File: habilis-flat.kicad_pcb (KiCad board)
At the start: 2 copper layers, 164.5 x 172.8 mm, 74 parts, among them J1 AudioJack4, SW1 MX, SW10 MX, SW11 MX, SW12 MX, SW13 MX, SW14 MX, SW15 MX, SW16 MX, SW17 MX, SW18 MX, SW19 MX, SW2 MX, SW20 MX, SW21 MX, SW22 MX, SW23 MX, SW24 MX, SW25 MX, SW26 MX, SW27 MX, SW28 MX, SW29 MX, SW3 MX, SW30 MX, SW31 MX, SW32 MX, SW33 MX, SW34 MX, SW35 MX, SW4 MX, SW5 MX, SW6 MX, SW7 MX, SW8 MX, SW9 MX, U1 ProMicro

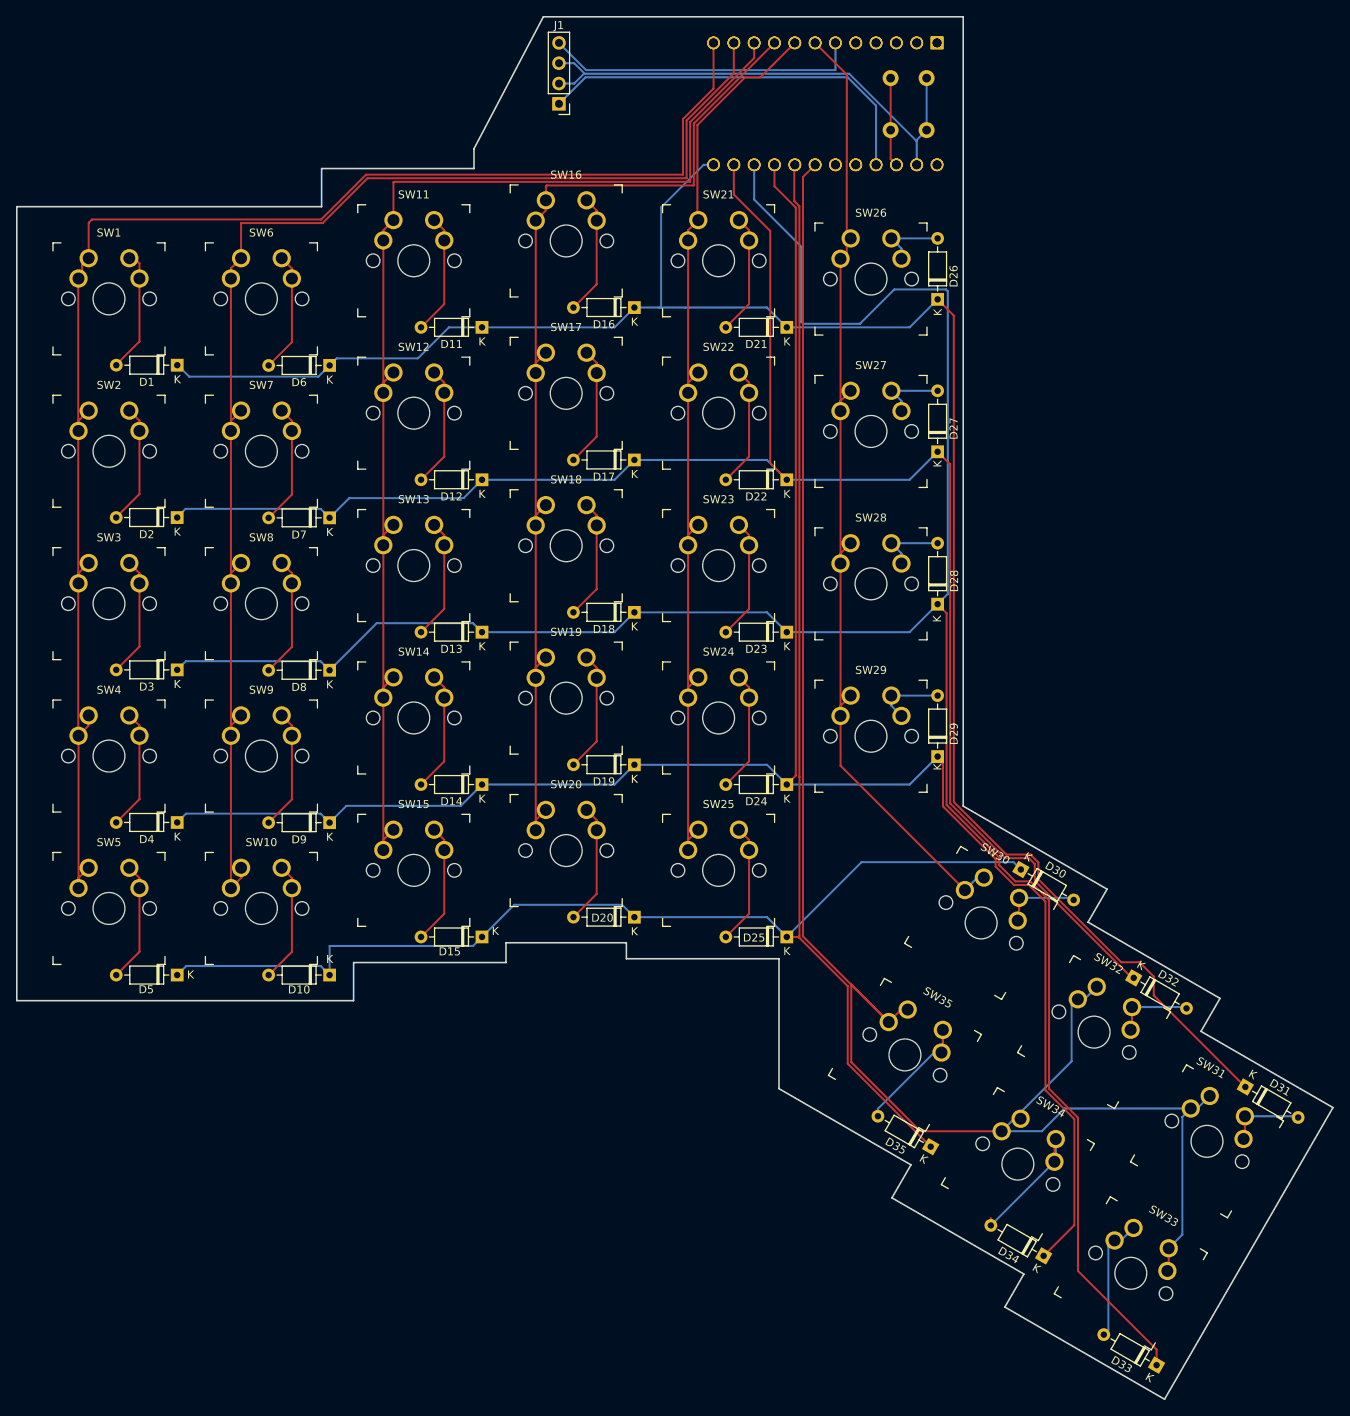
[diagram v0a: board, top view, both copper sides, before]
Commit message: Add mounting holes, simplify silkscreen
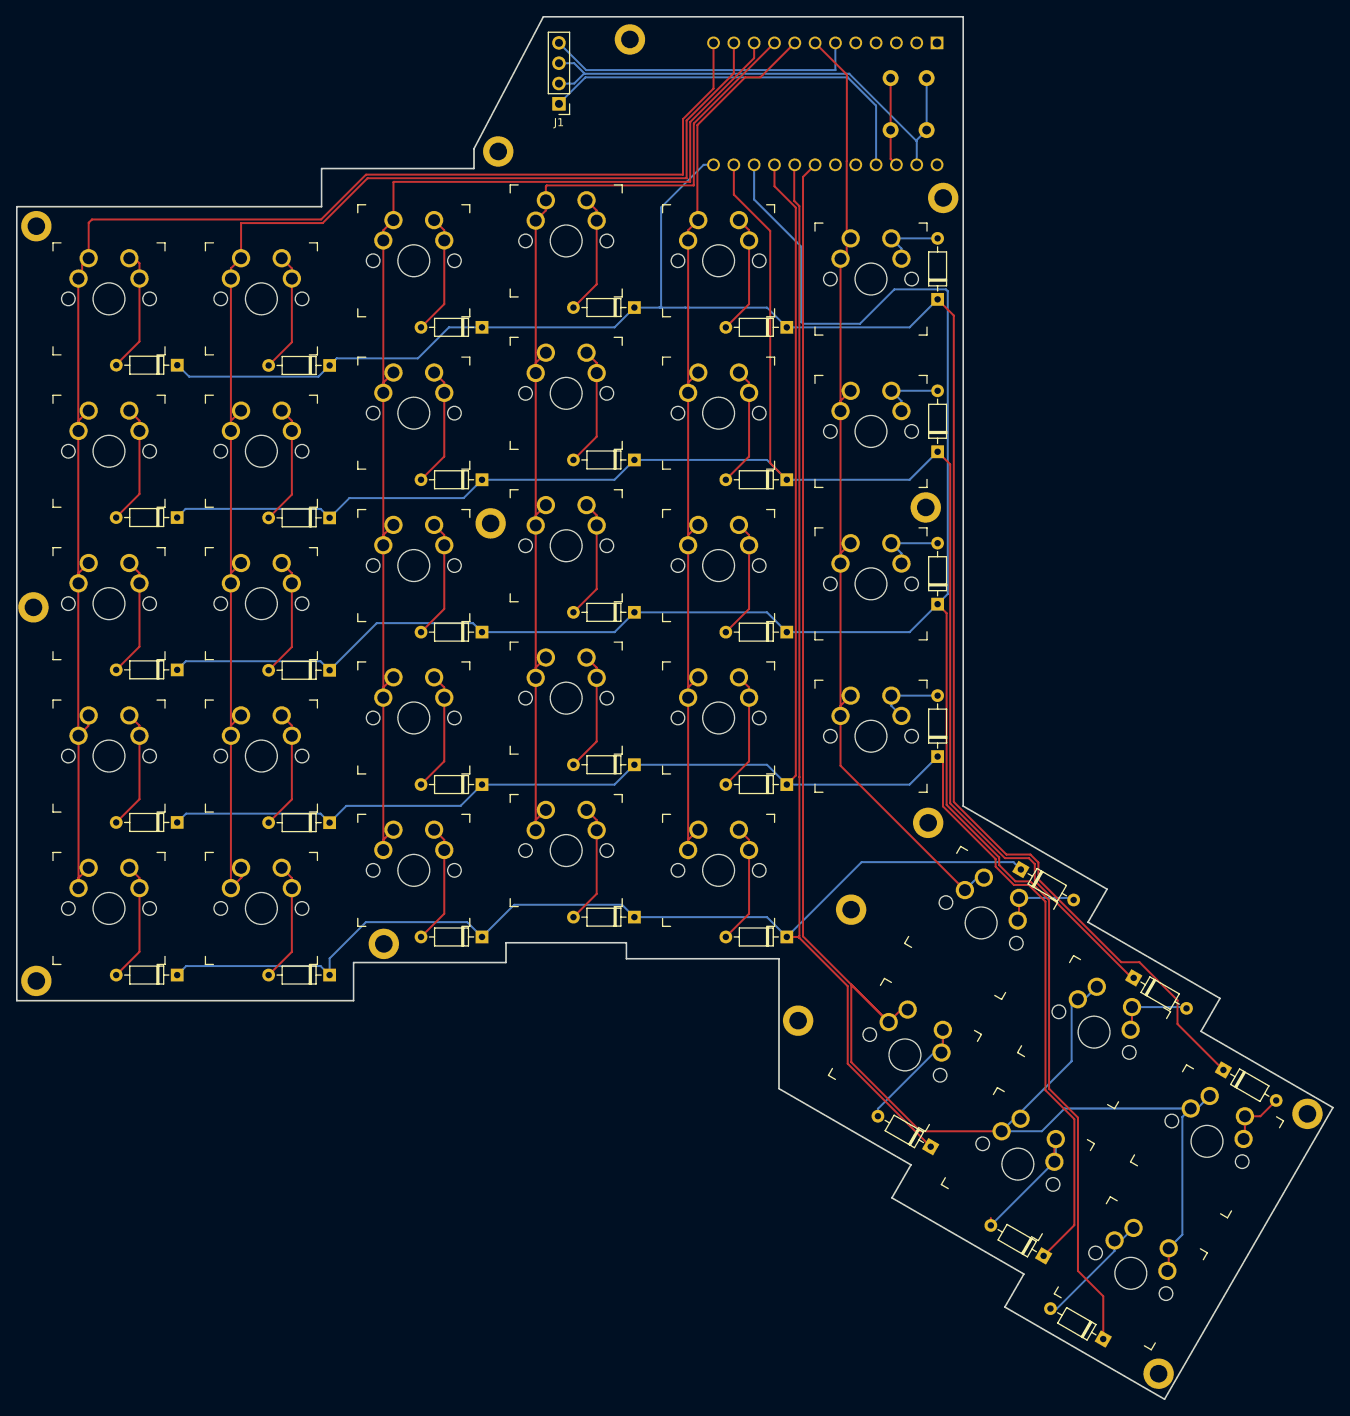
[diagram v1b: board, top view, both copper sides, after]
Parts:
- removed the U1 at (87.0, -19.3)
- added REF**: MountingHole_2.2mm_M2_DIN965_Pad_NO_Silkscreem, project-components:MountingHole_2.2mm_M2_DIN965_Pad_NO_Silkscreem, F.Cu at (99.6, 31.2)
- added REF**: MountingHole_2.2mm_M2_DIN965_Pad_NO_Silkscreem, project-components:MountingHole_2.2mm_M2_DIN965_Pad_NO_Silkscreem, F.Cu at (31.8, 85.7)
- added REF**: MountingHole_2.2mm_M2_DIN965_Pad_NO_Silkscreem, project-components:MountingHole_2.2mm_M2_DIN965_Pad_NO_Silkscreem, F.Cu at (99.9, 70.6)
- added REF**: MountingHole_2.2mm_M2_DIN965_Pad_NO_Silkscreem, project-components:MountingHole_2.2mm_M2_DIN965_Pad_NO_Silkscreem, F.Cu at (-11.6, -4.00)
- added REF**: MountingHole_2.2mm_M2_DIN965_Pad_NO_Silkscreem, project-components:MountingHole_2.2mm_M2_DIN965_Pad_NO_Silkscreem, F.Cu at (-11.6, 90.3)
- added REF**: MountingHole_2.2mm_M2_DIN965_Pad_NO_Silkscreem, project-components:MountingHole_2.2mm_M2_DIN965_Pad_NO_Silkscreem, F.Cu at (147.3, 107.0)
- added REF**: MountingHole_2.2mm_M2_DIN965_Pad_NO_Silkscreem, project-components:MountingHole_2.2mm_M2_DIN965_Pad_NO_Silkscreem, F.Cu at (46.1, -13.3)
- added REF**: MountingHole_2.2mm_M2_DIN965_Pad_NO_Silkscreem, project-components:MountingHole_2.2mm_M2_DIN965_Pad_NO_Silkscreem, F.Cu at (83.6, 95.3)
- added REF**: MountingHole_2.2mm_M2_DIN965_Pad_NO_Silkscreem, project-components:MountingHole_2.2mm_M2_DIN965_Pad_NO_Silkscreem, F.Cu at (128.7, 139.4)
- added REF**: MountingHole_2.2mm_M2_DIN965_Pad_NO_Silkscreem, project-components:MountingHole_2.2mm_M2_DIN965_Pad_NO_Silkscreem, F.Cu at (-12.0, 43.6)
- added REF**: MountingHole_2.2mm_M2_DIN965_Pad_NO_Silkscreem, project-components:MountingHole_2.2mm_M2_DIN965_Pad_NO_Silkscreem, F.Cu at (101.7, -7.53)
- added REF**: MountingHole_2.2mm_M2_DIN965_Pad_NO_Silkscreem, project-components:MountingHole_2.2mm_M2_DIN965_Pad_NO_Silkscreem, F.Cu at (45.2, 33.1)
- added REF**: MountingHole_2.2mm_M2_DIN965_Pad_NO_Silkscreem, project-components:MountingHole_2.2mm_M2_DIN965_Pad_NO_Silkscreem, F.Cu at (90.2, 81.4)
- added REF**: MountingHole_2.2mm_M2_DIN965_Pad_NO_Silkscreem, project-components:MountingHole_2.2mm_M2_DIN965_Pad_NO_Silkscreem, F.Cu at (62.6, -27.3)
- D1, D10, D11, D12, D13, D14, D15, D16, D17, D18, D19, D2, D20, D21, D22, D23, D24, D25, D26, D27, D28, D29, D3, D30, D31, D32, D33, D34, D35, D4, D5, D6, D7, D8, D9: footprint Diode_THT:D_DO-35_SOD27_P7.62mm_Horizontal -> project-components:D_DO-35_SOD27_P7.62mm_Horizontal
- moved D33 7.42 mm to (121.7, 135.1)
- moved D31 3.47 mm to (136.8, 101.5)
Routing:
- net Net-(D13-K): track 291.9 -> 285.9 mm
- net Net-(D1-K): track 240.8 -> 238.2 mm
- net Net-(D31-A): track 9.62 -> 7.63 mm
- net Net-(D10-K): track 249.6 -> 250.2 mm

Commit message: Duplicate TRRS header
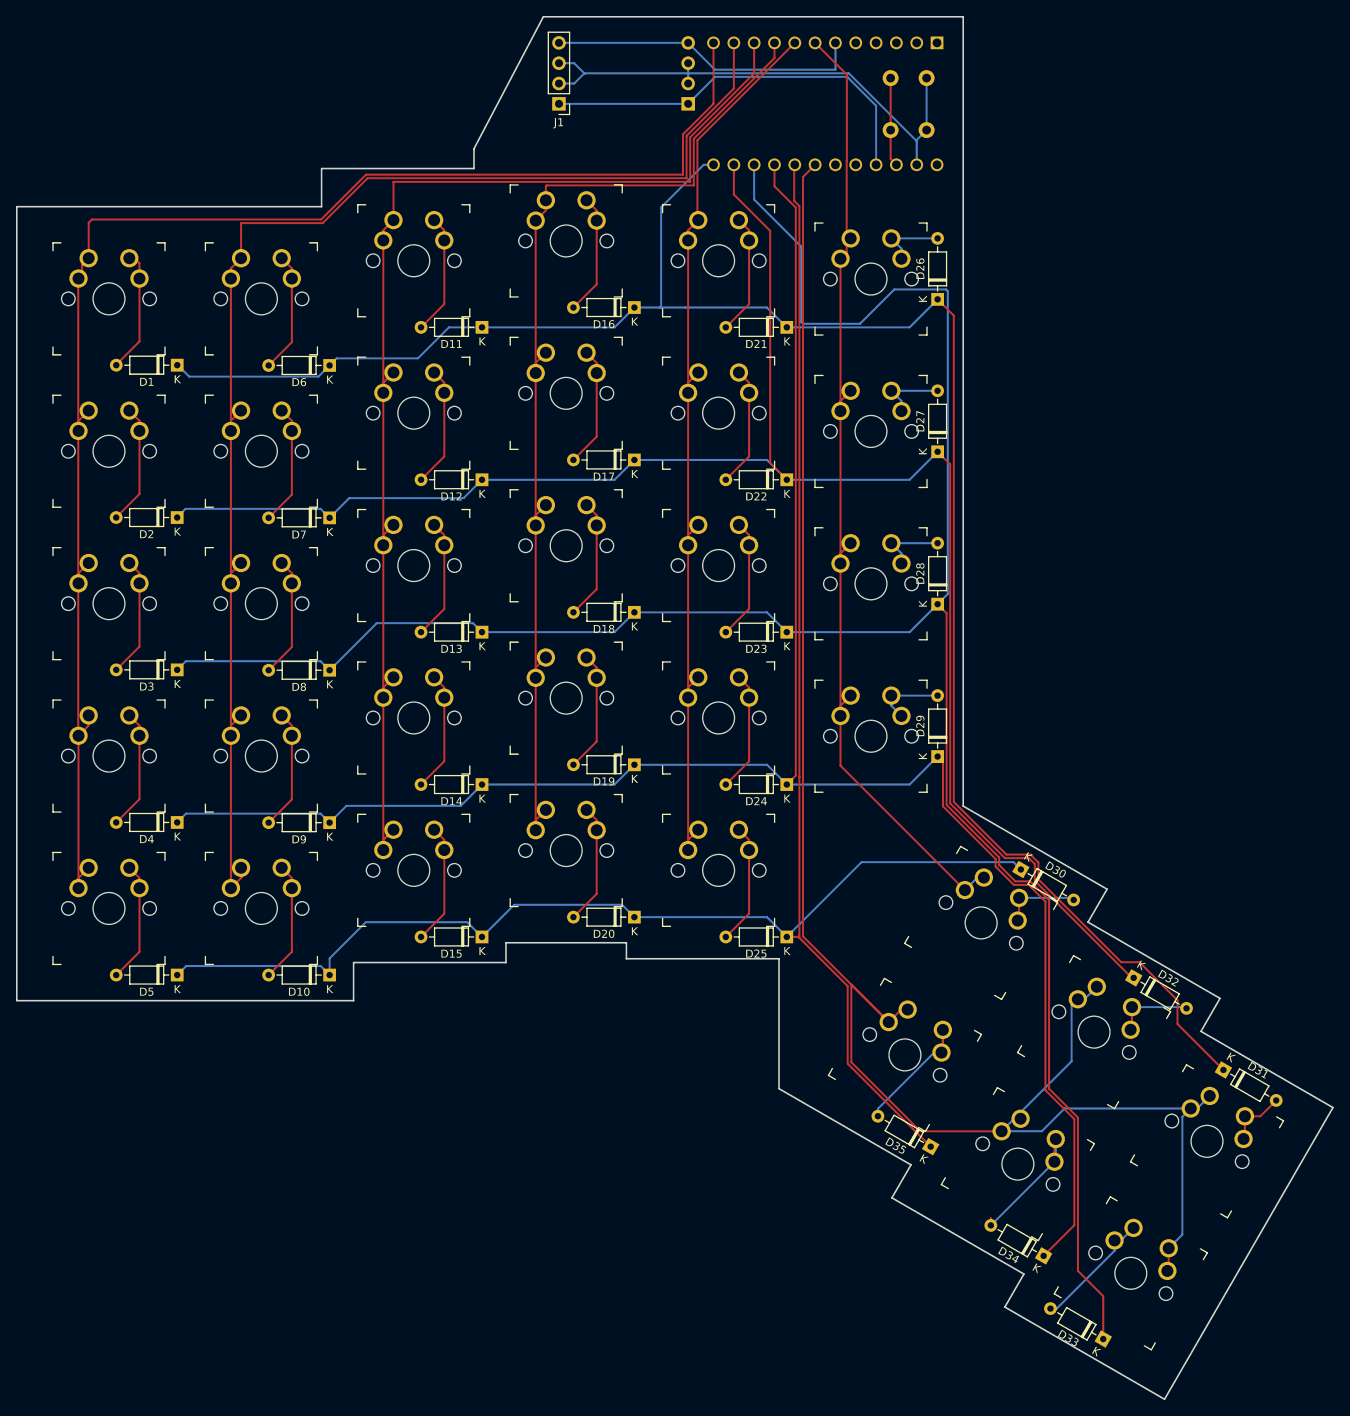
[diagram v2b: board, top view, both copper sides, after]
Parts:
- removed REF** (x14): MountingHole_2.2mm_M2_DIN965_Pad_NO_Silkscreem, project-components:MountingHole_2.2mm_M2_DIN965_Pad_NO_Silkscreem
- added J2: AudioJack4, project-components:Jack breakout board, B.Cu at (69.9, -19.3)
- D1, D10, D11, D12, D13, D14, D15, D16, D17, D18, D19, D2, D20, D21, D22, D23, D24, D25, D26, D27, D28, D29, D3, D30, D31, D32, D33, D34, D35, D4, D5, D6, D7, D8, D9: footprint project-components:D_DO-35_SOD27_P7.62mm_Horizontal -> Diode_THT:D_DO-35_SOD27_P7.62mm_Horizontal
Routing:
- net Net-(J1-PadR1): track 63.9 -> 66.5 mm
- net Net-(U1-C6): track 119.9 -> 118.8 mm

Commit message: Silkscreen cleanup
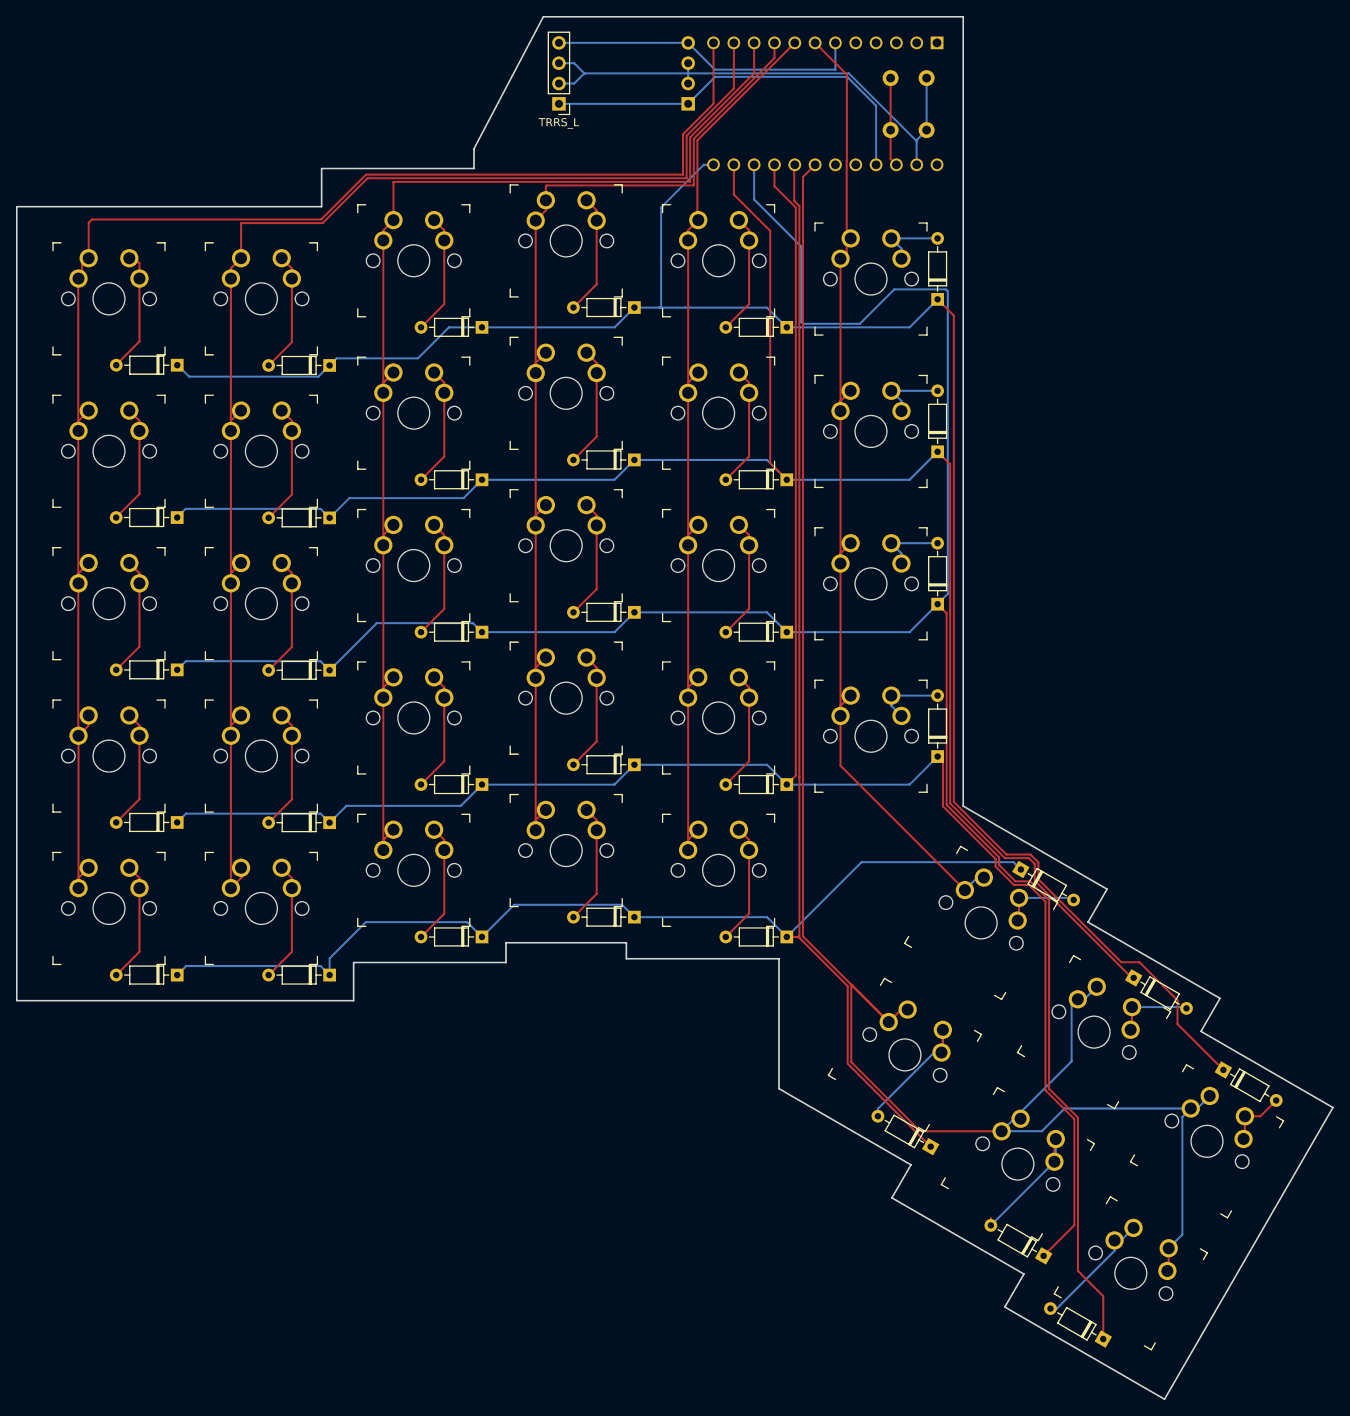
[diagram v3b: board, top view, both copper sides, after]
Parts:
- D1, D10, D11, D12, D13, D14, D15, D16, D17, D18, D19, D2, D20, D21, D22, D23, D24, D25, D26, D27, D28, D29, D3, D30, D31, D32, D33, D34, D35, D4, D5, D6, D7, D8, D9: footprint Diode_THT:D_DO-35_SOD27_P7.62mm_Horizontal -> project-components:D_DO-35_SOD27_P7.62mm_Horizontal
- renumbered J1 to TRRS_L, J2 to TRRS_R
